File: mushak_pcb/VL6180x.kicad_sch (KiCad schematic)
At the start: 9 parts, among them U4 VL6180XV0NR/1

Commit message: Add footprints
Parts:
- C29, C30: footprint (none) -> Capacitor_SMD:C_0805_2012Metric
- R14, R15: footprint (none) -> Resistor_SMD:R_0805_2012Metric
- TP43: footprint (none) -> TestPoint:TestPoint_Keystone_5019_Minature
- TP45: footprint (none) -> TestPoint:TestPoint_Pad_2.5x2.5mm
- U4: footprint LGA12R75P2X6_280X480X110 -> VL6180XV0NR_1:LGA12R75P2X6_280X480X110
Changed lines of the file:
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@@
     (property "Reference" "U4" (id 0) (at 147.574 80.645 0))
     (property "Value" "VL6180XV0NR/1" (id 1) (at 147.574 83.185 0))
-    (property "Footprint" "LGA12R75P2X6_280X480X110" (id 2) (at 147.574 93.98 0)
+    (property "Footprint" "VL6180XV0NR_1:LGA12R75P2X6_280X480X110" (id 2) (at 147.574 93.98 0)
       (effects (font (size 1.27 1.27)) (justify left bottom) hide)
     )
@@
       (effects (font (size 1.27 1.27)) (justify left))
     )
-    (property "Footprint" "" (id 2) (at 192.7352 98.044 0)
+    (property "Footprint" "Capacitor_SMD:C_0805_2012Metric" (id 2) (at 192.7352 98.044 0)
       (effects (font (size 1.27 1.27)) hide)
     )
@@
       (effects (font (size 1.27 1.27)) (justify left))
     )
-    (property "Footprint" "" (id 2) (at 122.428 91.44 0)
+    (property "Footprint" "TestPoint:TestPoint_Keystone_5019_Minature" (id 2) (at 122.428 91.44 0)
       (effects (font (size 1.27 1.27)) hide)
     )
@@
     (property "Reference" "R14" (id 0) (at 129.286 79.502 90))
     (property "Value" "4.7k" (id 1) (at 133.35 84.582 90))
-    (property "Footprint" "" (id 2) (at 131.318 84.074 90)
+    (property "Footprint" "Resistor_SMD:R_0805_2012Metric" (id 2) (at 131.318 84.074 90)
       (effects (font (size 1.27 1.27)) hide)
     )
@@
       (effects (font (size 1.27 1.27)) (justify left))
     )
-    (property "Footprint" "" (id 2) (at 169.672 112.522 0)
+    (property "Footprint" "TestPoint:TestPoint_Pad_2.5x2.5mm" (id 2) (at 169.672 112.522 0)
       (effects (font (size 1.27 1.27)) hide)
     )
@@
     (property "Reference" "R15" (id 0) (at 143.256 69.85 90))
     (property "Value" "4.7k" (id 1) (at 143.256 72.39 90))
-    (property "Footprint" "" (id 2) (at 143.256 77.724 90)
+    (property "Footprint" "Resistor_SMD:R_0805_2012Metric" (id 2) (at 143.256 77.724 90)
       (effects (font (size 1.27 1.27)) hide)
     )
@@
       (effects (font (size 1.27 1.27)) (justify left))
     )
-    (property "Footprint" "" (id 2) (at 183.0832 98.044 0)
+    (property "Footprint" "Capacitor_SMD:C_0805_2012Metric" (id 2) (at 183.0832 98.044 0)
       (effects (font (size 1.27 1.27)) hide)
     )

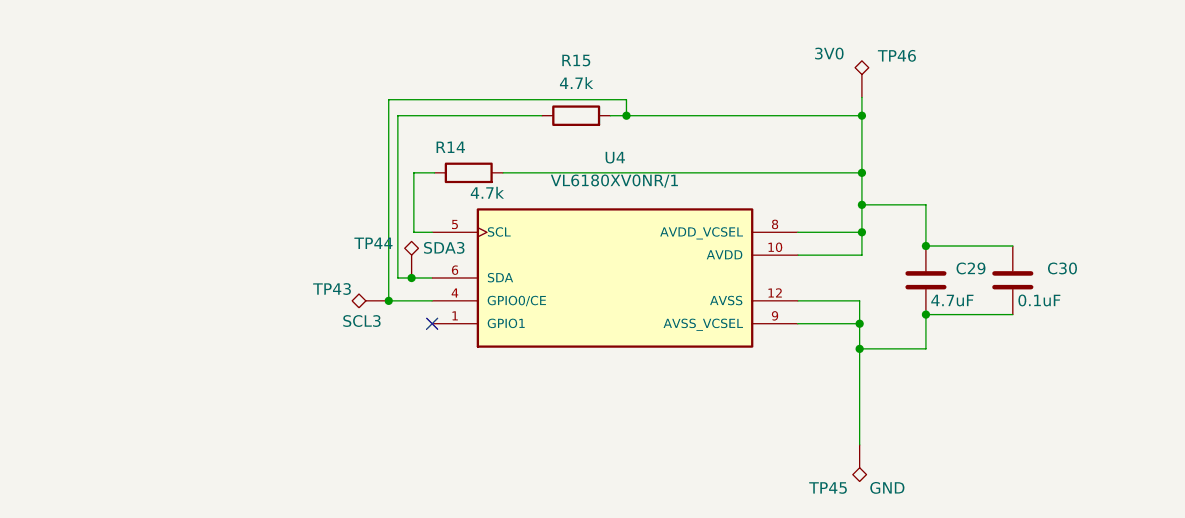
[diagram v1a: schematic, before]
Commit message: Update Schematics and footprints for sensors
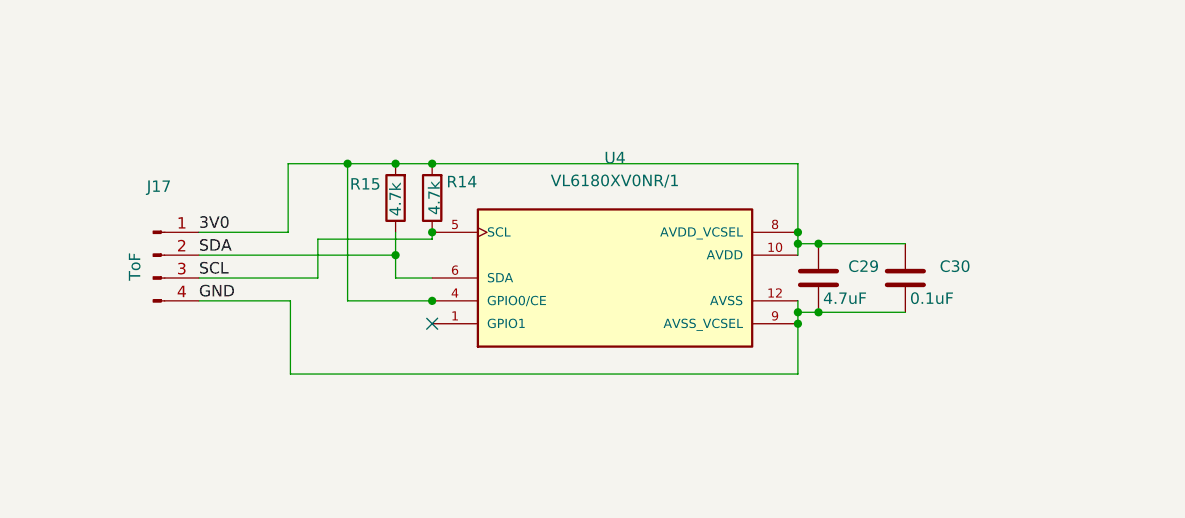
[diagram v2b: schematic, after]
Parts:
- removed TP43: SCL3, TestPoint:TestPoint_Keystone_5019_Minature, symbol Connector:TestPoint_Alt
- removed TP44: SDA3, TestPoint:TestPoint_Keystone_5019_Minature, symbol Connector:TestPoint_Alt
- removed TP45: GND, TestPoint:TestPoint_Pad_2.5x2.5mm, symbol Connector:TestPoint_Alt
- removed TP46: 3V0, TestPoint:TestPoint_Pad_2.5x2.5mm, symbol Connector:TestPoint_Alt
- added J17: ToF, mushak_mount_footprint:STAND_SLAVE_04, symbol Connector:Conn_01x04_Male
- C29, C30: footprint Capacitor_SMD:C_0805_2012Metric -> Capacitor_SMD:C_0402_1005Metric
- R14, R15: footprint Resistor_SMD:R_0805_2012Metric -> Resistor_SMD:R_0402_1005Metric
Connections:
- net 3V0: now reaches C29.1, C30.1, R14.2, R15.2, U4.10 (AVDD), U4.4 (GPIO0/CE), U4.8 (AVDD_VCSEL)
- net 3V0: now also J17.1 (Pin_1)
- net GND: now reaches C29.2, C30.2, U4.12 (AVSS), U4.9 (AVSS_VCSEL)
- net GND: now also J17.4 (Pin_4)
- net SCL: now reaches R14.1, U4.5 (SCL)
- net SCL: now also J17.3 (Pin_3)
- net SDA: now reaches R15.1, U4.6 (SDA)
- net SDA: now also J17.2 (Pin_2)
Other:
- moved on the sheet: C29, C30, R14, R15

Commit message: changed footprints of capacitors and resistors
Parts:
- C30: footprint Capacitor_SMD:C_0402_1005Metric -> Capacitor_SMD:C_0201_0603Metric
- R14, R15: footprint Resistor_SMD:R_0402_1005Metric -> Resistor_SMD:R_0201_0603Metric
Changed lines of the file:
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@@
       (effects (font (size 1.27 1.27)) (justify left))
     )
-    (property "Footprint" "Capacitor_SMD:C_0402_1005Metric" (id 2) (at 180.7972 97.79 0)
+    (property "Footprint" "Capacitor_SMD:C_0201_0603Metric" (id 2) (at 180.7972 97.79 0)
       (effects (font (size 1.27 1.27)) hide)
     )
@@
     (property "Reference" "R14" (id 0) (at 130.556 83.312 0))
     (property "Value" "4.7k" (id 1) (at 127.508 85.09 90))
-    (property "Footprint" "Resistor_SMD:R_0402_1005Metric" (id 2) (at 129.032 85.09 90)
+    (property "Footprint" "Resistor_SMD:R_0201_0603Metric" (id 2) (at 129.032 85.09 90)
       (effects (font (size 1.27 1.27)) hide)
     )
@@
       (effects (font (size 1.27 1.27)) (justify right))
     )
-    (property "Footprint" "Resistor_SMD:R_0402_1005Metric" (id 2) (at 124.968 85.09 90)
+    (property "Footprint" "Resistor_SMD:R_0201_0603Metric" (id 2) (at 124.968 85.09 90)
       (effects (font (size 1.27 1.27)) hide)
     )

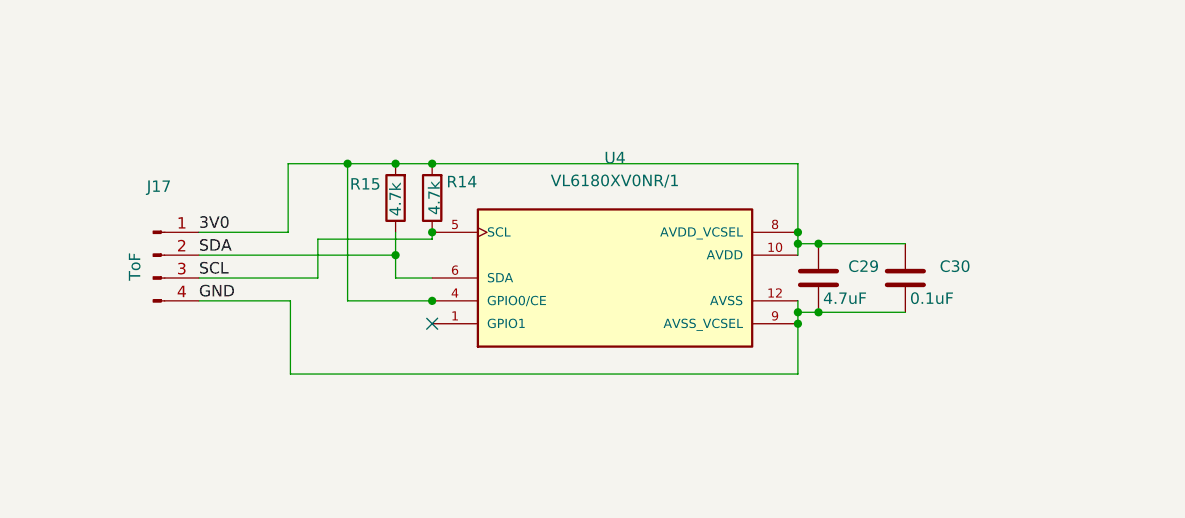
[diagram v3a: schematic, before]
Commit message: corrected encoder and motor driver schematics
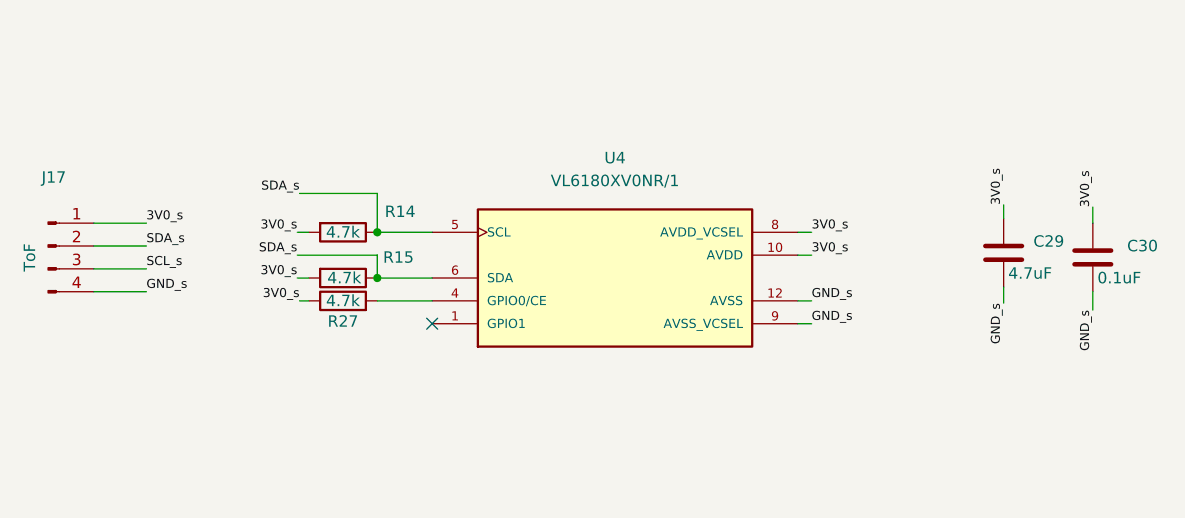
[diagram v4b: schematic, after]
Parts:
- added R27: 4.7k, symbol Device:R
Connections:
- net SDA is gone; now on net SDA_s: J17.2 (Pin_2), R15.1, U4.6 (SDA)
- net 3V0 renamed 3V0_s
- net 3V0_s: now also R27.1; no longer U4.4 (GPIO0/CE)
- net GND renamed GND_s
- net SCL renamed SDA_s
- net SDA_s: no longer J17.3 (Pin_3)
- new net: R27.2, U4.4 (GPIO0/CE)
- new net SCL_s: J17.3 (Pin_3)
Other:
- moved on the sheet: C29, C30, J17, R14, R15

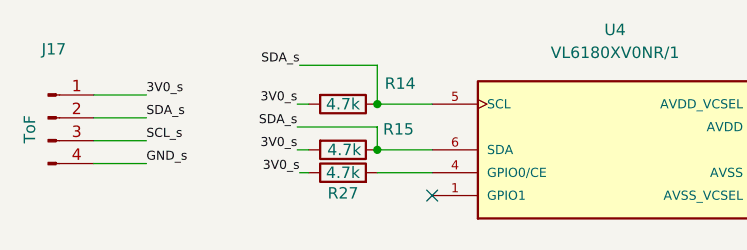
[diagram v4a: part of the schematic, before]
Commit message: VL6180x part routed
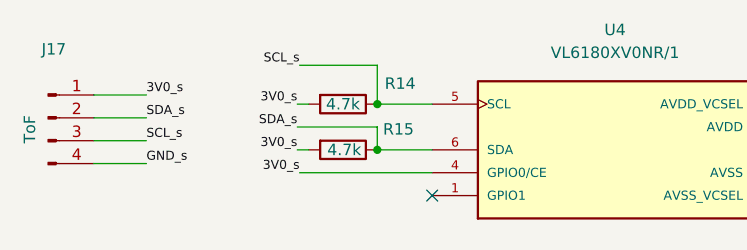
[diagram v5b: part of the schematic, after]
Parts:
- removed R27: 4.7k, symbol Device:R
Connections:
- net 3V0_s: now also U4.4 (GPIO0/CE)
- net SCL_s: now also R14.1, U4.5 (SCL)
- net SDA_s: no longer R14.1, U4.5 (SCL)
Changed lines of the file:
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@@
     (stroke (width 0) (type default) (color 0 0 0 0))
   )
-  (wire (pts (xy 112.522 96.52) (xy 113.538 96.52))
-    (stroke (width 0) (type default) (color 0 0 0 0))
-  )
-  (wire (pts (xy 121.158 96.52) (xy 127.254 96.52))
+  (wire (pts (xy 112.522 96.52) (xy 127.254 96.52))
     (stroke (width 0) (type default) (color 0 0 0 0))
   )
@@
     (effects (font (size 1 1)) (justify right bottom))
   )
-  (label "SDA_s" (at 112.522 84.582 180)
+  (label "SCL_s" (at 112.522 84.582 180)
     (effects (font (size 1 1)) (justify right bottom))
   )
@@
       (effects (font (size 1.27 1.27)) hide)
     )
-    (pin "1")
-    (pin "2")
-  )
-  (symbol (lib_id "Device:R") (at 117.348 96.52 90) (unit 1)
-    (in_bom yes) (on_board yes)
-    (property "Reference" "R27" (id 0) (at 117.348 98.806 90))
-    (property "Value" "4.7k" (id 1) (at 117.348 96.52 90))
-    (property "Footprint" "" (id 2) (at 117.348 98.298 90)
-      (effects (font (size 1.27 1.27)) hide)
-    )
-    (property "Datasheet" "~" (id 3) (at 117.348 96.52 0)
-      (effects (font (size 1.27 1.27)) hide)
-    )

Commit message: changed footprint of passive components
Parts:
- C29: footprint Capacitor_SMD:C_0402_1005Metric -> Capacitor_SMD:C_0603_1608Metric
- C30: footprint Capacitor_SMD:C_0201_0603Metric -> Capacitor_SMD:C_0402_1005Metric
- R14, R15: footprint Resistor_SMD:R_0201_0603Metric -> Resistor_SMD:R_0402_1005Metric
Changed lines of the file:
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@@
       (effects (font (size 1.27 1.27)) (justify left))
     )
-    (property "Footprint" "Capacitor_SMD:C_0201_0603Metric" (id 2) (at 201.6252 95.504 0)
+    (property "Footprint" "Capacitor_SMD:C_0402_1005Metric" (id 2) (at 201.6252 95.504 0)
       (effects (font (size 1.27 1.27)) hide)
     )
@@
     (property "Reference" "R14" (id 0) (at 123.698 86.614 90))
     (property "Value" "4.7k" (id 1) (at 117.348 88.9 90))
-    (property "Footprint" "Resistor_SMD:R_0201_0603Metric" (id 2) (at 117.348 87.122 90)
+    (property "Footprint" "Resistor_SMD:R_0402_1005Metric" (id 2) (at 117.348 87.122 90)
       (effects (font (size 1.27 1.27)) hide)
     )
@@
       (effects (font (size 1.27 1.27)) (justify right))
     )
-    (property "Footprint" "Resistor_SMD:R_0201_0603Metric" (id 2) (at 117.348 92.202 90)
+    (property "Footprint" "Resistor_SMD:R_0402_1005Metric" (id 2) (at 117.348 92.202 90)
       (effects (font (size 1.27 1.27)) hide)
     )
@@
       (effects (font (size 1.27 1.27)) (justify left))
     )
-    (property "Footprint" "Capacitor_SMD:C_0402_1005Metric" (id 2) (at 191.7192 94.996 0)
+    (property "Footprint" "Capacitor_SMD:C_0603_1608Metric" (id 2) (at 191.7192 94.996 0)
       (effects (font (size 1.27 1.27)) hide)
     )

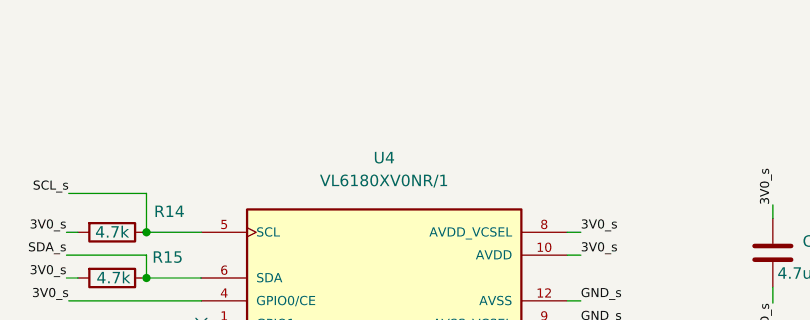
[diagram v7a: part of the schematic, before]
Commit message: changed oscilattor placement
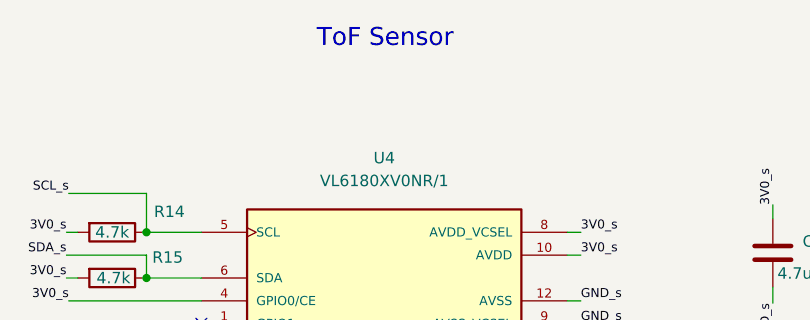
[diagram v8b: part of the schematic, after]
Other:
- note added: "ToF Sensor"
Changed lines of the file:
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@@
     (stroke (width 0) (type default) (color 0 0 0 0))
+  )
+  (text "ToF Sensor" (at 140.081 68.58 0)
+    (effects (font (size 2 2)) (justify left bottom))
   )
   (label "SCL_s" (at 95.504 92.964 0)
